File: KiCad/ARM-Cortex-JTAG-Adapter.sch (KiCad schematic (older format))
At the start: 4 parts, among them J1 Data, J2 Power

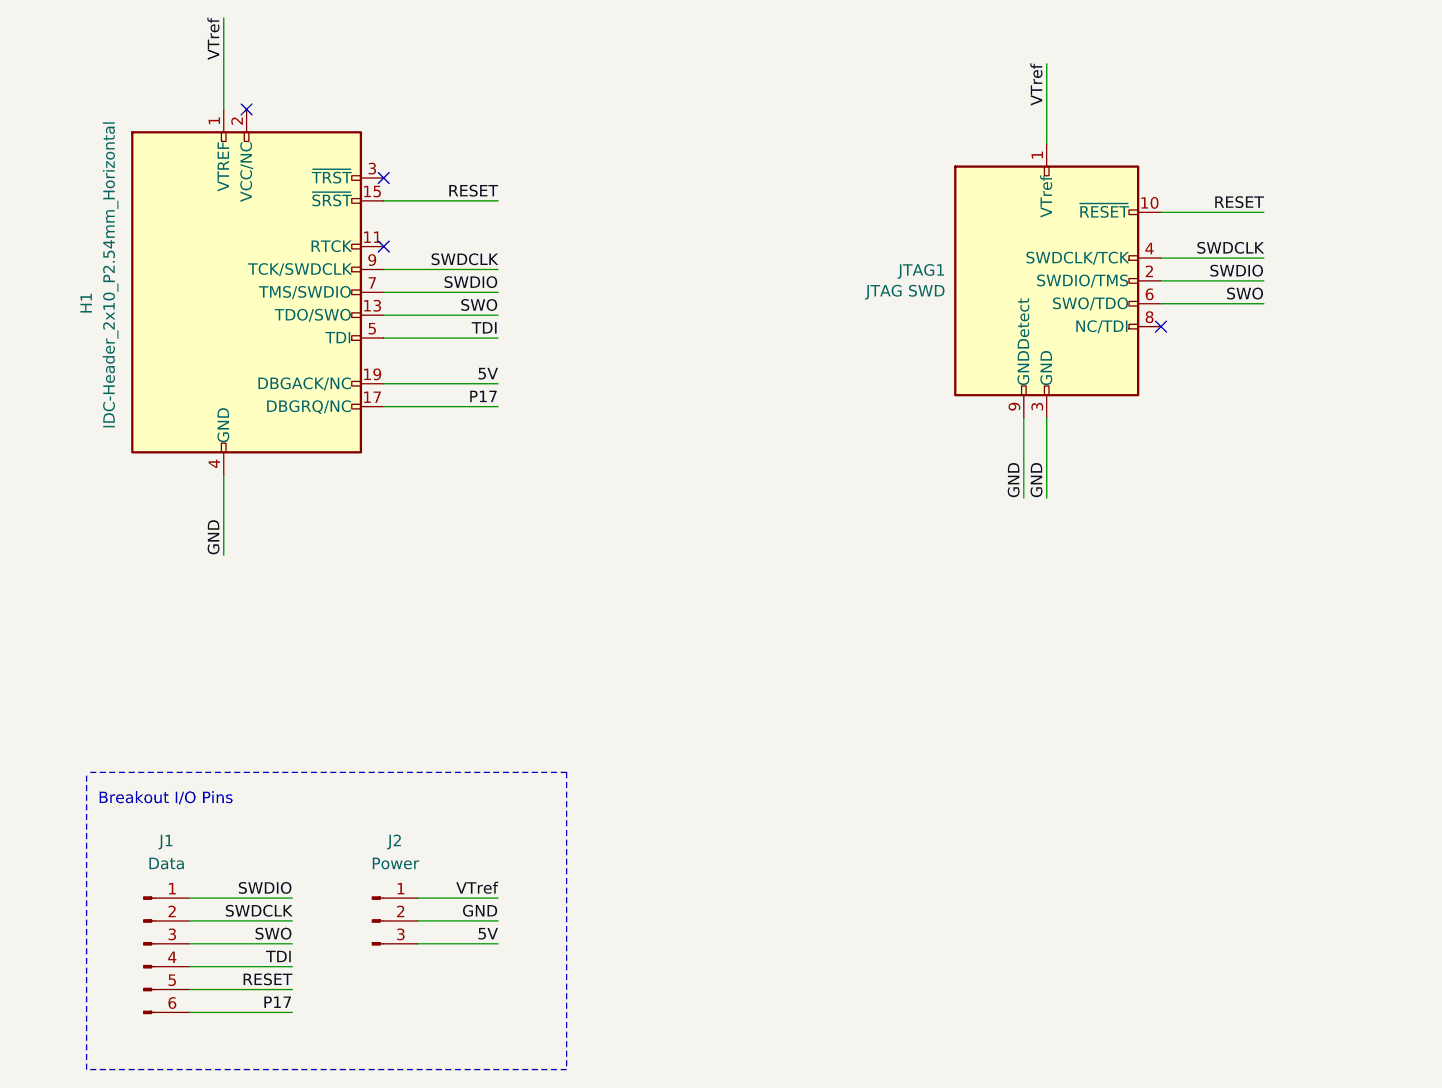
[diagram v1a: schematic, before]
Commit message: Revising schematic for optional TDI pin.
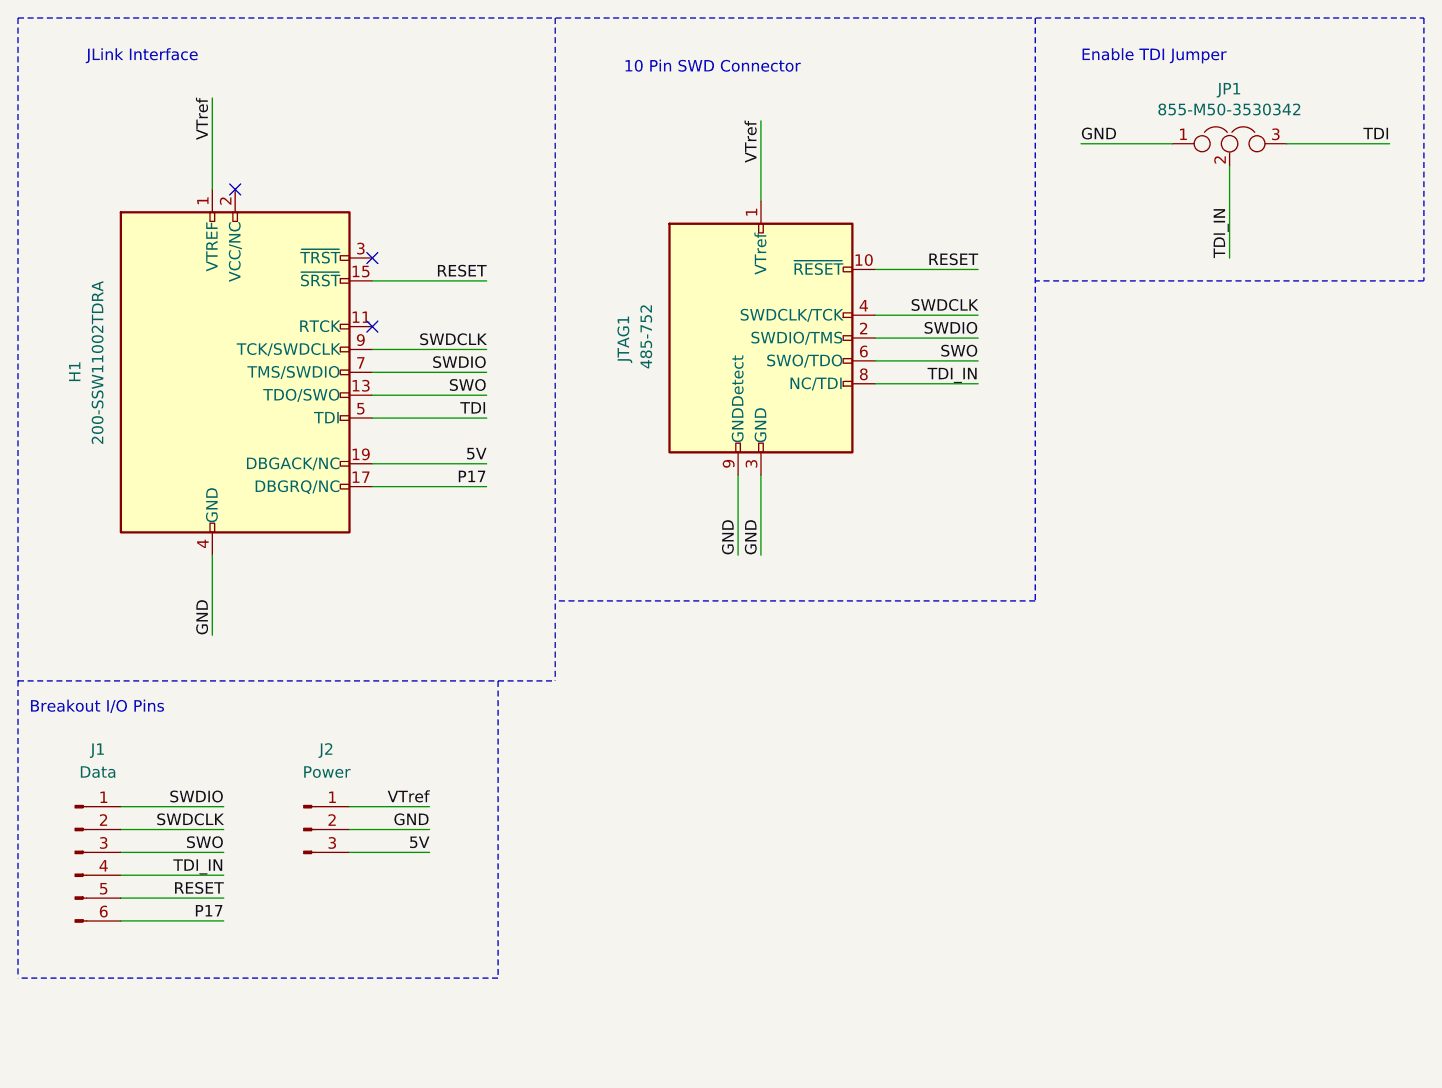
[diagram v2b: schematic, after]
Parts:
- added JP1: 855-M50-3530342, Connector_PinHeader_1.27mm:PinHeader_1x03_P1.27mm_Vertical, symbol Device:Jumper_NC_Dual
- H1: value IDC-Header_2x10_P2.54mm_Horizontal -> 200-SSW11002TDRA
- JTAG1: value JTAG SWD -> 485-752; footprint Connector_PinHeader_1.27mm:PinHeader_2x05_P1.27mm_Vertical -> Connector_PinHeader_1.27mm:PinHeader_2x05_P1.27mm_Vertical_SMD
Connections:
- net GND: now also JP1.1
- net TDI: now also JP1.3; no longer J1.4 (Pin_4)
- net TDI_IN: now reaches JTAG1.8 (NC/TDI)
- net TDI_IN: now also J1.4 (Pin_4), JP1.2
- no-connect marks 4 -> 3
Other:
- note added: "10 Pin SWD Connector"
- note added: "Enable TDI Jumper"
- note added: "JLink Interface"
- moved on the sheet: H1, J1, J2, JTAG1
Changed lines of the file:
@@
 encoding utf-8
 Sheet 1 1
-Title ""
-Date ""
-Rev ""
-Comp ""
-Comment1 ""
+Title "ARM Cortex-M/A JTAG Adapter"
+Date "2020-09-23"
+Rev "0.1A"
+Comp "https://github.com/jeff-winn/ARM-Cortex-JTAG-Adapter"
+Comment1 "For more information please visit the project website:"
 Comment2 ""
 Comment3 ""
 Comment4 ""
 $EndDescr
+Text Label 4450 1200 3    50   ~ 0
+VTref
+Wire Wire Line
+	4950 2050 5400 2050
+Text Label 5400 2050 2    50   ~ 0
+SWDCLK
+Wire Wire Line
+	4950 2150 5400 2150
+Text Label 5400 2150 2    50   ~ 0
+SWDIO
+Wire Wire Line
+	4950 2250 5400 2250
+Text Label 5400 2250 2    50   ~ 0
+SWO
+Wire Wire Line
+	4950 1850 5400 1850
+Text Label 5400 1850 2    50   ~ 0
+RESET
+$Comp
+L Connector:Conn_01x03_Male J2
+U 1 1 5F65A72D
+P 2450 4300
+F 0 "J2" H 2550 4650 50  0000 C CNN
+F 1 "Power" H 2550 4550 50  0000 C CNN
+F 2 "Connector_PinHeader_2.54mm:PinHeader_1x03_P2.54mm_Vertical" H 2450 4300 50  0001 C CNN
+F 3 "~" H 2450 4300 50  0001 C CNN
+	1    2450 4300
+	1    0    0    -1
+$EndComp
+Wire Wire Line
+	2650 4200 3000 4200
+Text Label 3000 4400 2    50   ~ 0
+5V
+Wire Wire Line
+	2650 4300 3000 4300
+Text Label 3000 4300 2    50   ~ 0
+GND
+Wire Wire Line
+	2650 4400 3000 4400
+Text Label 3000 4200 2    50   ~ 0
+VTref
+Wire Wire Line
+	1650 4200 2100 4200
+Text Label 2100 4300 2    50   ~ 0
+SWDCLK
+Wire Wire Line
+	1650 4300 2100 4300
+Text Label 2100 4200 2    50   ~ 0
+SWDIO
+Wire Wire Line
+	1650 4400 2100 4400
+Text Label 2100 4400 2    50   ~ 0
+SWO
+Wire Wire Line
+	1650 4500 2100 4500
+Text Label 2100 4500 2    50   ~ 0
+TDI_IN
+$Comp
+L Connector:Conn_ARM_JTAG_SWD_20 H1
+U 1 1 5F661477
+P 2150 2300
+F 0 "H1" V 1450 2350 50  0000 R CNN
+F 1 "200-SSW11002TDRA" V 1550 2700 50  0000 R CNN
+F 2 "Connector_IDC:IDC-Header_2x10_P2.54mm_Horizontal" H 2600 1250 50  0001 L TNN
+F 3 "http://infocenter.arm.com/help/topic/com.arm.doc.dui0499b/DUI0499B_system_design_reference.pdf" V 1800 1050 50  0001 C CNN
+	1    2150 2300
+	1    0    0    -1
+$EndComp
+Wire Wire Line
+	2050 1500 2050 1100
+Text Label 2050 1100 3    50   ~ 0
+VTref
+NoConn ~ 2150 1500
+NoConn ~ 2750 1800
+Wire Wire Line
+	2750 1900 3250 1900
+Text Label 3250 1900 2    50   ~ 0
+RESET
+Wire Wire Line
+	2750 2200 3250 2200
+Text Label 3250 2200 2    50   ~ 0
+SWDCLK
+Wire Wire Line
+	2750 2300 3250 2300
+Text Label 3250 2300 2    50   ~ 0
+SWDIO
+Wire Wire Line
+	2750 2400 3250 2400
+Text Label 3250 2400 2    50   ~ 0
+SWO
+Wire Wire Line
+	2050 3100 2050 3450
+Text Label 2050 3450 1    50   ~ 0
+GND
+Wire Wire Line
+	2750 2700 3250 2700
+Text Label 3250 2700 2    50   ~ 0
+5V
+Wire Wire Line
+	2750 2500 3250 2500
+Text Label 3250 2500 2    50   ~ 0
+TDI
+Wire Wire Line
+	4450 2750 4450 3100
+Text Label 4450 3100 1    50   ~ 0
+GND
+NoConn ~ 2750 2100
+Wire Wire Line
+	4350 2750 4350 3100
+Text Label 4350 3100 1    50   ~ 0
+GND
+Wire Wire Line
+	2750 2800 3250 2800
+Text Label 3250 2800 2    50   ~ 0
+P17
+Wire Wire Line
+	1650 4600 2100 4600
+Text Label 2100 4600 2    50   ~ 0
+RESET
+Wire Wire Line
+	1650 4700 2100 4700
+Text Label 2100 4700 2    50   ~ 0
+P17
+$Comp
+L Connector:Conn_01x06_Male J1
+U 1 1 5F67F15F
+P 1450 4400
+F 0 "J1" H 1550 4850 50  0000 C CNN
+F 1 "Data" H 1550 4750 50  0000 C CNN
+F 2 "Connector_PinHeader_2.54mm:PinHeader_1x06_P2.54mm_Vertical" H 1450 4400 50  0001 C CNN
+F 3 "~" H 1450 4400 50  0001 C CNN
+	1    1450 4400
+	1    0    0    -1
+$EndComp
+Wire Notes Line
+	3300 3650 3300 4950
+Wire Notes Line
+	3300 4950 1200 4950
+Text Notes 1250 3800 0    50   ~ 0
+Breakout I/O Pins
+Wire Wire Line
+	4450 1200 4450 1550
 $Comp
 L Connector:Conn_ARM_JTAG_SWD_10 JTAG1
 U 1 1 5F64FD35
-P 5700 1900
-F 0 "JTAG1" H 5257 1946 50  0000 R CNN
-F 1 "JTAG SWD" H 5257 1855 50  0000 R CNN
-F 2 "Connector_PinHeader_1.27mm:PinHeader_2x05_P1.27mm_Vertical" H 5700 1900 50  0001 C CNN
-F 3 "http://infocenter.arm.com/help/topic/com.arm.doc.ddi0314h/DDI0314H_coresight_components_trm.pdf" V 5350 650 50  0001 C CNN
-	1    5700 1900
-	1    0    0    -1
-$EndComp
-Wire Wire Line
-	5700 950  5700 1300
-Text Label 5700 950  3    50   ~ 0
-VTref
-Wire Wire Line
-	6200 1800 6650 1800
-Text Label 6650 1800 2    50   ~ 0
-SWDCLK
-Wire Wire Line
-	6200 1900 6650 1900
-Text Label 6650 1900 2    50   ~ 0
-SWDIO
-Wire Wire Line
-	6200 2000 6650 2000
-Text Label 6650 2000 2    50   ~ 0
-SWO
-NoConn ~ 6200 2100
-Wire Wire Line
-	6200 1600 6650 1600
-Text Label 6650 1600 2    50   ~ 0
-RESET
-$Comp
-L Connector:Conn_01x03_Male J2
-U 1 1 5F65A72D
-P 2750 4700
-F 0 "J2" H 2850 5050 50  0000 C CNN
-F 1 "Power" H 2850 4950 50  0000 C CNN
-F 2 "Connector_PinHeader_2.54mm:PinHeader_1x03_P2.54mm_Vertical" H 2750 4700 50  0001 C CNN
-F 3 "~" H 2750 4700 50  0001 C CNN
-	1    2750 4700
-	1    0    0    -1
-$EndComp
-Wire Wire Line
-	2950 4600 3300 4600
-Text Label 3300 4800 2    50   ~ 0
-5V
-Wire Wire Line
-	2950 4700 3300 4700
-Text Label 3300 4700 2    50   ~ 0
-GND
-Wire Wire Line
-	2950 4800 3300 4800
-Text Label 3300 4600 2    50   ~ 0
-VTref
-Wire Wire Line
-	1950 4600 2400 4600
-Text Label 2400 4700 2    50   ~ 0
-SWDCLK
-Wire Wire Line
-	1950 4700 2400 4700
-Text Label 2400 4600 2    50   ~ 0
-SWDIO
-Wire Wire Line
-	1950 4800 2400 4800
-Text Label 2400 4800 2    50   ~ 0
-SWO
-Wire Wire Line
-	1950 4900 2400 4900
-Text Label 2400 4900 2    50   ~ 0
+P 4450 2150
+F 0 "JTAG1" V 3850 2250 50  0000 R CNN
+F 1 "485-752" V 3950 2300 50  0000 R CNN
+F 2 "Connector_PinHeader_1.27mm:PinHeader_2x05_P1.27mm_Vertical_SMD" H 4450 2150 50  0001 C CNN
+F 3 "http://infocenter.arm.com/help/topic/com.arm.doc.ddi0314h/DDI0314H_coresight_components_trm.pdf" V 4100 900 50  0001 C CNN
+	1    4450 2150
+	1    0    0    -1
+$EndComp
+$Comp
+L Device:Jumper_NC_Dual JP1
+U 1 1 5F696F05
+P 6500 1300
+F 0 "JP1" H 6500 1539 50  0000 C CNN
+F 1 "855-M50-3530342" H 6500 1448 50  0000 C CNN
+F 2 "Connector_PinHeader_1.27mm:PinHeader_1x03_P1.27mm_Vertical" H 6500 1300 50  0001 C CNN
+F 3 "~" H 6500 1300 50  0001 C CNN
+	1    6500 1300
+	1    0    0    -1
+$EndComp
+Wire Wire Line
+	6250 1300 5850 1300
+Text Label 5850 1300 0    50   ~ 0
+GND
+Wire Wire Line
+	6750 1300 7200 1300
+Text Label 7200 1300 2    50   ~ 0
 TDI
-$Comp
-L Connector:Conn_ARM_JTAG_SWD_20 H1
-U 1 1 5F661477
-P 2200 1950
-F 0 "H1" V 1500 1950 50  0000 R CNN
-F 1 "IDC-Header_2x10_P2.54mm_Horizontal" V 1600 2700 50  0000 R CNN
-F 2 "Connector_IDC:IDC-Header_2x10_P2.54mm_Horizontal" H 2650 900 50  0001 L TNN
-F 3 "http://infocenter.arm.com/help/topic/com.arm.doc.dui0499b/DUI0499B_system_design_reference.pdf" V 1850 700 50  0001 C CNN
-	1    2200 1950
-	1    0    0    -1
-$EndComp
-Wire Wire Line
-	2100 1150 2100 750
-Text Label 2100 750  3    50   ~ 0
-VTref
-NoConn ~ 2200 1150
-NoConn ~ 2800 1450
-Wire Wire Line
-	2800 1550 3300 1550
-Text Label 3300 1550 2    50   ~ 0
-RESET
-Wire Wire Line
-	2800 1850 3300 1850
-Text Label 3300 1850 2    50   ~ 0
-SWDCLK
-Wire Wire Line
-	2800 1950 3300 1950
-Text Label 3300 1950 2    50   ~ 0
-SWDIO
-Wire Wire Line
-	2800 2050 3300 2050
-Text Label 3300 2050 2    50   ~ 0
-SWO
-Wire Wire Line
-	2100 2750 2100 3100
-Text Label 2100 3100 1    50   ~ 0
-GND
-Wire Wire Line
-	2800 2350 3300 2350
-Text Label 3300 2350 2    50   ~ 0
-5V
-Wire Wire Line
-	2800 2150 3300 2150
-Text Label 3300 2150 2    50   ~ 0
-TDI
-Wire Wire Line
-	5700 2500 5700 2850
-Text Label 5700 2850 1    50   ~ 0
-GND
-NoConn ~ 2800 1750
-Wire Wire Line
-	5600 2500 5600 2850
-Text Label 5600 2850 1    50   ~ 0
-GND
-Wire Wire Line
-	2800 2450 3300 2450
-Text Label 3300 2450 2    50   ~ 0
-P17
-Wire Wire Line
-	1950 5000 2400 5000
-Text Label 2400 5000 2    50   ~ 0
-RESET
-Wire Wire Line
-	1950 5100 2400 5100
-Text Label 2400 5100 2    50   ~ 0
-P17
-$Comp
-L Connector:Conn_01x06_Male J1
-U 1 1 5F67F15F
-P 1750 4800
-F 0 "J1" H 1850 5250 50  0000 C CNN
-F 1 "Data" H 1850 5150 50  0000 C CNN
-F 2 "Connector_PinHeader_2.54mm:PinHeader_1x06_P2.54mm_Vertical" H 1750 4800 50  0001 C CNN
-F 3 "~" H 1750 4800 50  0001 C CNN
-	1    1750 4800
-	1    0    0    -1
-$EndComp
-Wire Notes Line
-	3600 4050 3600 5350
-Wire Notes Line
-	3600 5350 1500 5350
-Wire Notes Line
-	1500 5350 1500 4050
-Wire Notes Line
-	3600 4050 1500 4050
-Text Notes 1550 4200 0    50   ~ 0
-Breakout I/O Pins
+Wire Wire Line
+	6500 1400 6500 1800
+Text Label 6500 1800 1    50   ~ 0
+TDI_IN
+Wire Wire Line
+	4950 2350 5400 2350
+Text Label 5400 2350 2    50   ~ 0
+TDI_IN
+Text Notes 5850 950  0    50   ~ 0
+Enable TDI Jumper
+Wire Notes Line
+	7350 750  7350 1900
+Wire Notes Line
+	7350 1900 5650 1900
+Text Notes 1500 950  0    50   ~ 0
+JLink Interface
+Text Notes 3850 1000 0    50   ~ 0
+10 Pin SWD Connector
+Wire Notes Line
+	5650 3300 3550 3300
+Wire Notes Line
+	3550 750  3550 3650
+Wire Notes Line
+	1200 750  1200 4950
+Wire Notes Line
+	1200 3650 3550 3650
+Wire Notes Line
+	5650 750  5650 3300
+Wire Notes Line
+	1200 750  7350 750
 $EndSCHEMATC

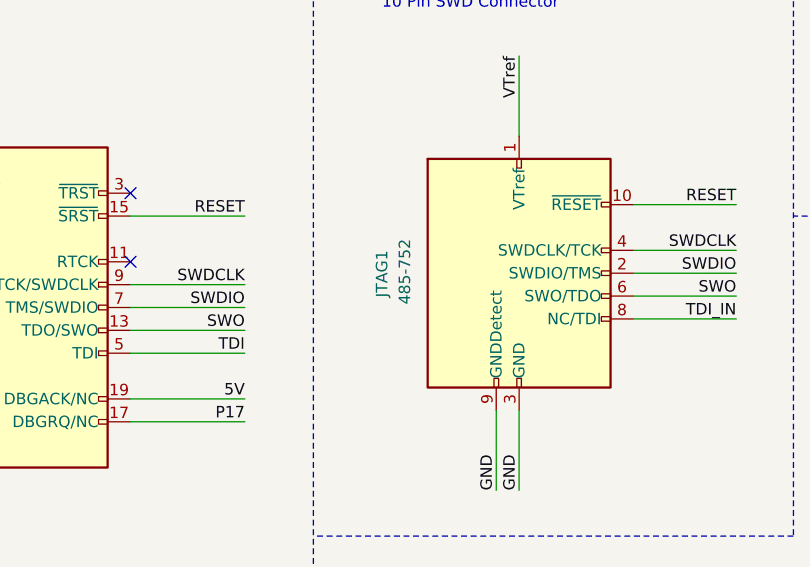
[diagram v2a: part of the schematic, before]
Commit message: Replacing connector type for JTAG1.
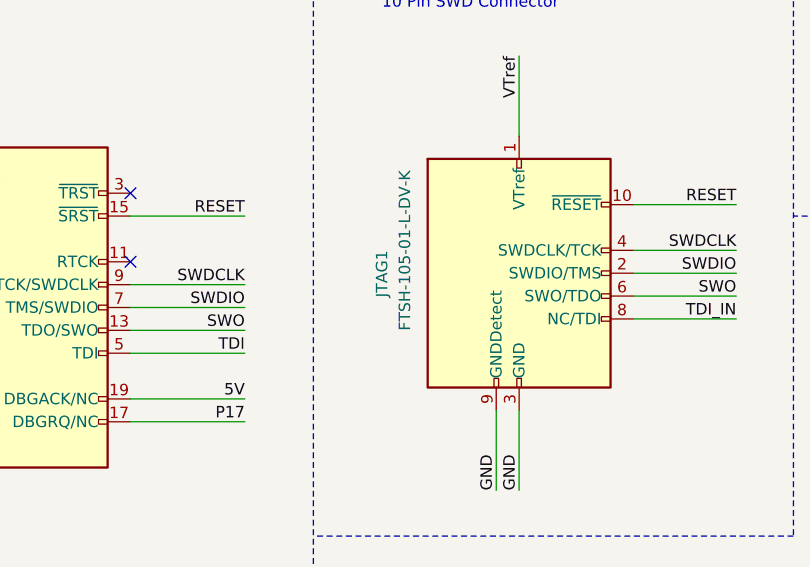
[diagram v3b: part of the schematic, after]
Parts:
- JTAG1: value 485-752 -> FTSH-105-01-L-DV-K; footprint Connector_PinHeader_1.27mm:PinHeader_2x05_P1.27mm_Vertical_SMD -> (Local):SAMTEC-FTSH-105-01-X-DV
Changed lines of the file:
@@
 P 4450 2150
 F 0 "JTAG1" V 3850 2250 50  0000 R CNN
-F 1 "485-752" V 3950 2300 50  0000 R CNN
-F 2 "Connector_PinHeader_1.27mm:PinHeader_2x05_P1.27mm_Vertical_SMD" H 4450 2150 50  0001 C CNN
+F 1 "FTSH-105-01-L-DV-K" V 3950 2600 50  0000 R CNN
+F 2 "(Local):SAMTEC-FTSH-105-01-X-DV" H 4450 2150 50  0001 C CNN
 F 3 "http://infocenter.arm.com/help/topic/com.arm.doc.ddi0314h/DDI0314H_coresight_components_trm.pdf" V 4100 900 50  0001 C CNN
 	1    4450 2150

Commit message: Updates.
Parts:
- removed JP1: 855-M50-3530342, Connector_PinHeader_1.27mm:PinHeader_1x03_P1.27mm_Vertical, symbol Device:Jumper_NC_Dual
- added JP1: 855-M50-3530342, Connector_PinHeader_2.54mm:PinHeader_1x02_P2.54mm_Vertical, symbol Device:Jumper
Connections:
- net TDI: now also JP1.2
- net TDI_IN: now also JP1.1
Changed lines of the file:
@@
-	1    0    0    -1
-$EndComp
-$Comp
-L Device:Jumper_NC_Dual JP1
-U 1 1 5F696F05
-P 6500 1300
-F 0 "JP1" H 6500 1539 50  0000 C CNN
-F 1 "855-M50-3530342" H 6500 1448 50  0000 C CNN
-F 2 "Connector_PinHeader_1.27mm:PinHeader_1x03_P1.27mm_Vertical" H 6500 1300 50  0001 C CNN
-F 3 "~" H 6500 1300 50  0001 C CNN
-	1    6500 1300
 	1    0    0    -1
 $EndComp
 Wire Wire Line
-	6250 1300 5850 1300
-Text Label 5850 1300 0    50   ~ 0
-GND
-Wire Wire Line
-	6750 1300 7200 1300
-Text Label 7200 1300 2    50   ~ 0
+	6800 1400 7250 1400
+Text Label 7250 1400 2    50   ~ 0
 TDI
-Wire Wire Line
-	6500 1400 6500 1800
-Text Label 6500 1800 1    50   ~ 0
-TDI_IN
 Wire Wire Line
 	4950 2350 5400 2350
@@
 Enable TDI Jumper
 Wire Notes Line
-	7350 750  7350 1900
+	7350 750  7350 1800
 Wire Notes Line
-	7350 1900 5650 1900
+	7350 1800 5650 1800
 Text Notes 1500 950  0    50   ~ 0
 JLink Interface
@@
 Wire Notes Line
 	1200 750  7350 750
+$Comp
+L Device:Jumper JP1
+U 1 1 5F73C045
+P 6500 1400
+F 0 "JP1" H 6500 1664 50  0000 C CNN
+F 1 "855-M50-3530342" H 6500 1573 50  0000 C CNN
+F 2 "Connector_PinHeader_2.54mm:PinHeader_1x02_P2.54mm_Vertical" H 6500 1400 50  0001 C CNN
+F 3 "~" H 6500 1400 50  0001 C CNN
+	1    6500 1400
+	1    0    0    -1
+$EndComp
+Wire Wire Line
+	5800 1400 6200 1400
+Text Label 5800 1400 0    50   ~ 0
+TDI_IN
 $EndSCHEMATC
